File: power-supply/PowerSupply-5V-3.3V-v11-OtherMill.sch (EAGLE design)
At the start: 19 parts, among them J1 POWER_JACK, J3 VCC, J4 GND, J5 NC1, J6 NC2, U1 LM317

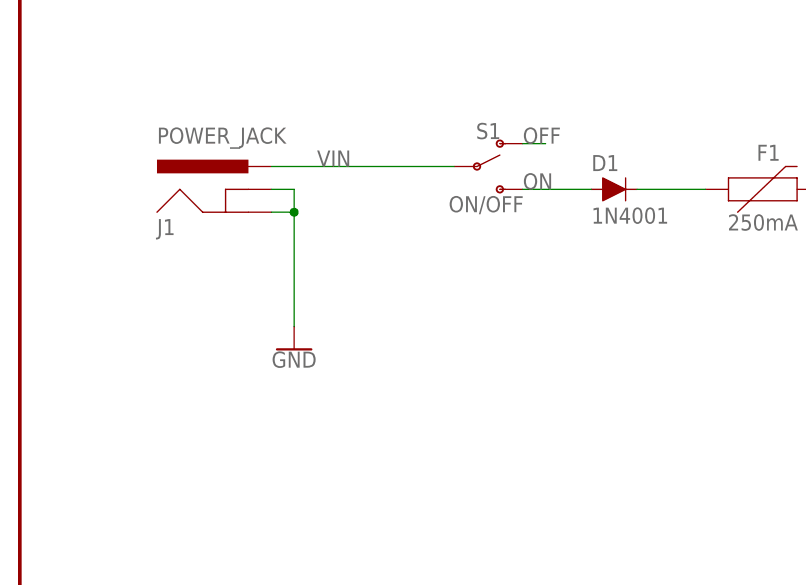
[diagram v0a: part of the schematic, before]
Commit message: Add raw voltage source
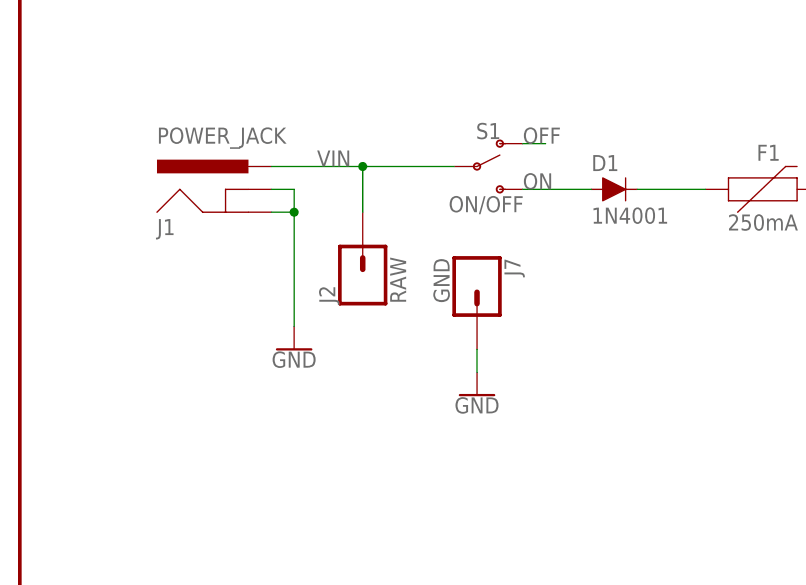
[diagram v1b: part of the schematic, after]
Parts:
- added J2: RAW, SparkFun-Connectors:CONN_01
- added J7: GND, SparkFun-Connectors:CONN_01
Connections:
- net GND: now also J7.1
- net VIN: now also J2.1
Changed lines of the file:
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@@
 <setting verticaltext="up"/>
 </settings>
-<grid distance="0.1" unitdist="inch" unit="inch" style="lines" multiple="1" display="yes" altdistance="0.01" altunitdist="inch" altunit="inch"/>
+<grid distance="0.1" unitdist="inch" unit="inch" style="lines" multiple="1" display="no" altdistance="0.01" altunitdist="inch" altunit="inch"/>
 <layers>
 <layer number="1" name="Top" color="4" fill="1" visible="no" active="no"/>
@@
 <part name="J5" library="SparkFun-Connectors" deviceset="CONN_01" device="" value="NC1"/>
 <part name="J6" library="SparkFun-Connectors" deviceset="CONN_01" device="" value="NC2"/>
+<part name="J2" library="SparkFun-Connectors" deviceset="CONN_01" device="" value="RAW"/>
+<part name="J7" library="SparkFun-Connectors" deviceset="CONN_01" device="" value="GND"/>
+<part name="GND2" library="SparkFun-PowerSymbols" deviceset="GND" device=""/>
 </parts>
 <sheets>
@@
 <instance part="J5" gate="G$1" x="93.98" y="71.12"/>
 <instance part="J6" gate="G$1" x="93.98" y="55.88"/>
+<instance part="J2" gate="G$1" x="38.1" y="124.46" rot="R90"/>
+<instance part="J7" gate="G$1" x="50.8" y="124.46" rot="R270"/>
+<instance part="GND2" gate="1" x="50.8" y="111.76"/>
 </instances>
 <busses>
@@
 <pinref part="J1" gate="G$1" pin="PWR"/>
 <pinref part="S1" gate="1" pin="P"/>
-<wire x1="27.94" y1="137.16" x2="48.26" y2="137.16" width="0.1524" layer="91"/>
+<wire x1="27.94" y1="137.16" x2="38.1" y2="137.16" width="0.1524" layer="91"/>
 <label x="33.02" y="137.16" size="1.778" layer="95"/>
+<pinref part="J2" gate="G$1" pin="1"/>
+<wire x1="38.1" y1="137.16" x2="48.26" y2="137.16" width="0.1524" layer="91"/>
+<wire x1="38.1" y1="137.16" x2="38.1" y2="132.08" width="0.1524" layer="91"/>
+<junction x="38.1" y="137.16"/>
 </segment>
 </net>
@@
 <label x="76.2" y="55.88" size="1.778" layer="95"/>
 </segment>
+<segment>
+<pinref part="J7" gate="G$1" pin="1"/>
+<pinref part="GND2" gate="1" pin="GND"/>
+<wire x1="50.8" y1="114.3" x2="50.8" y2="116.84" width="0.1524" layer="91"/>
+</segment>
 </net>
